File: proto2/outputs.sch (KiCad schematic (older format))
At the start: 36 parts, among them U1 AQY282SX, U10 AQY282SX, U11 AQY282SX, U12 AQY282SX, U2 AQY282SX, U3 AQY282SX, U4 AQY282SX, U5 AQY282SX, U6 AQY282SX, U7 AQY282SX, U8 AQY282SX, U9 AQY282SX

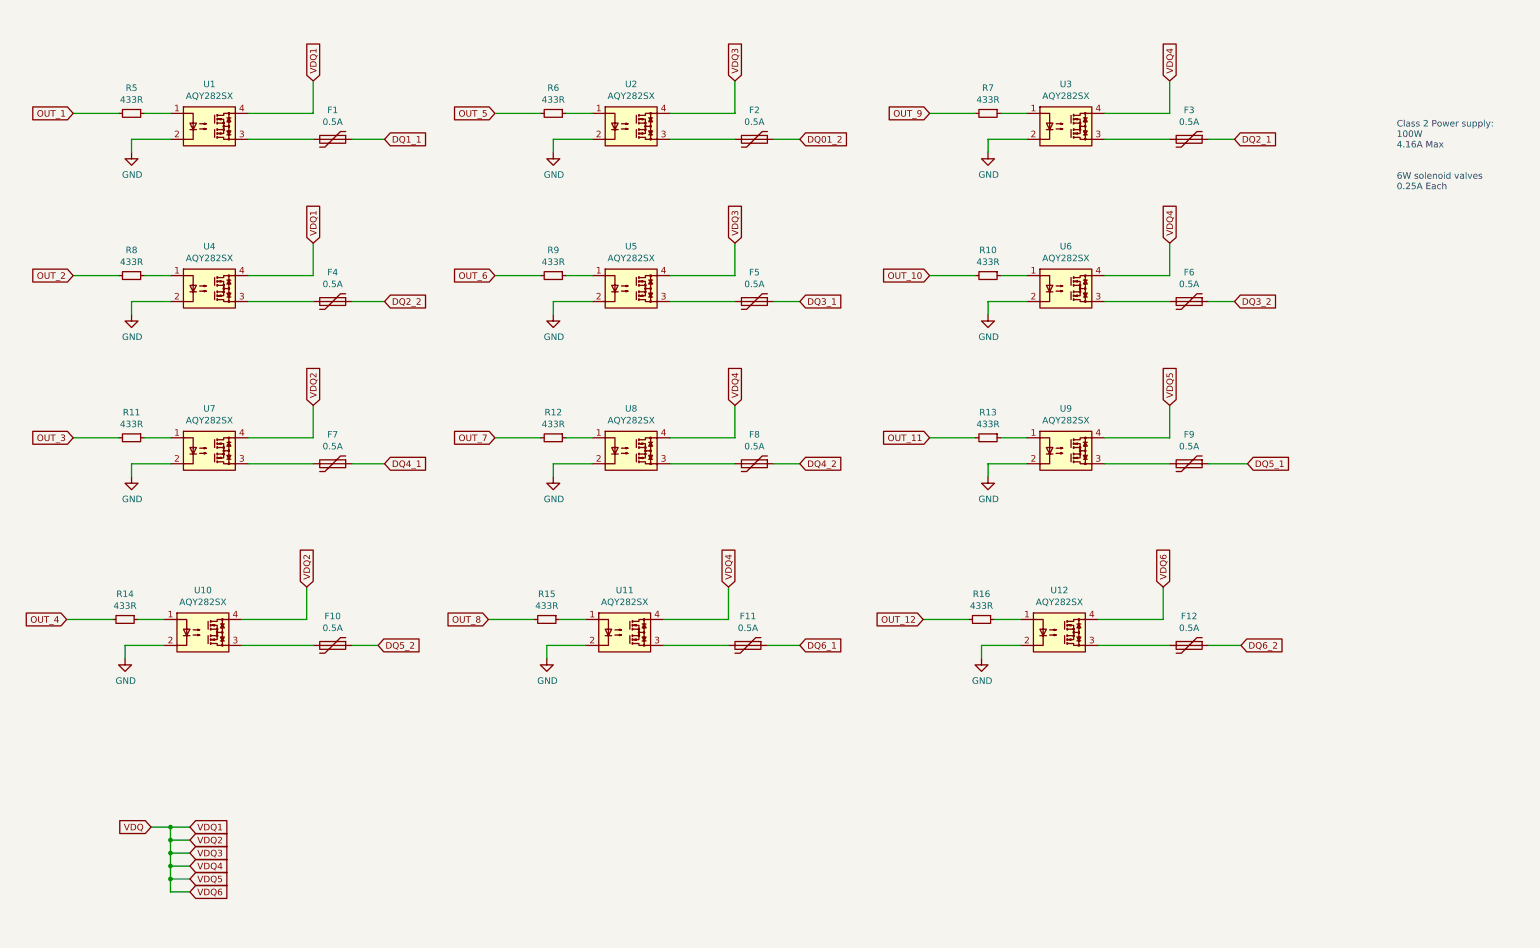
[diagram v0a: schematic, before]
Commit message: Routed Board.
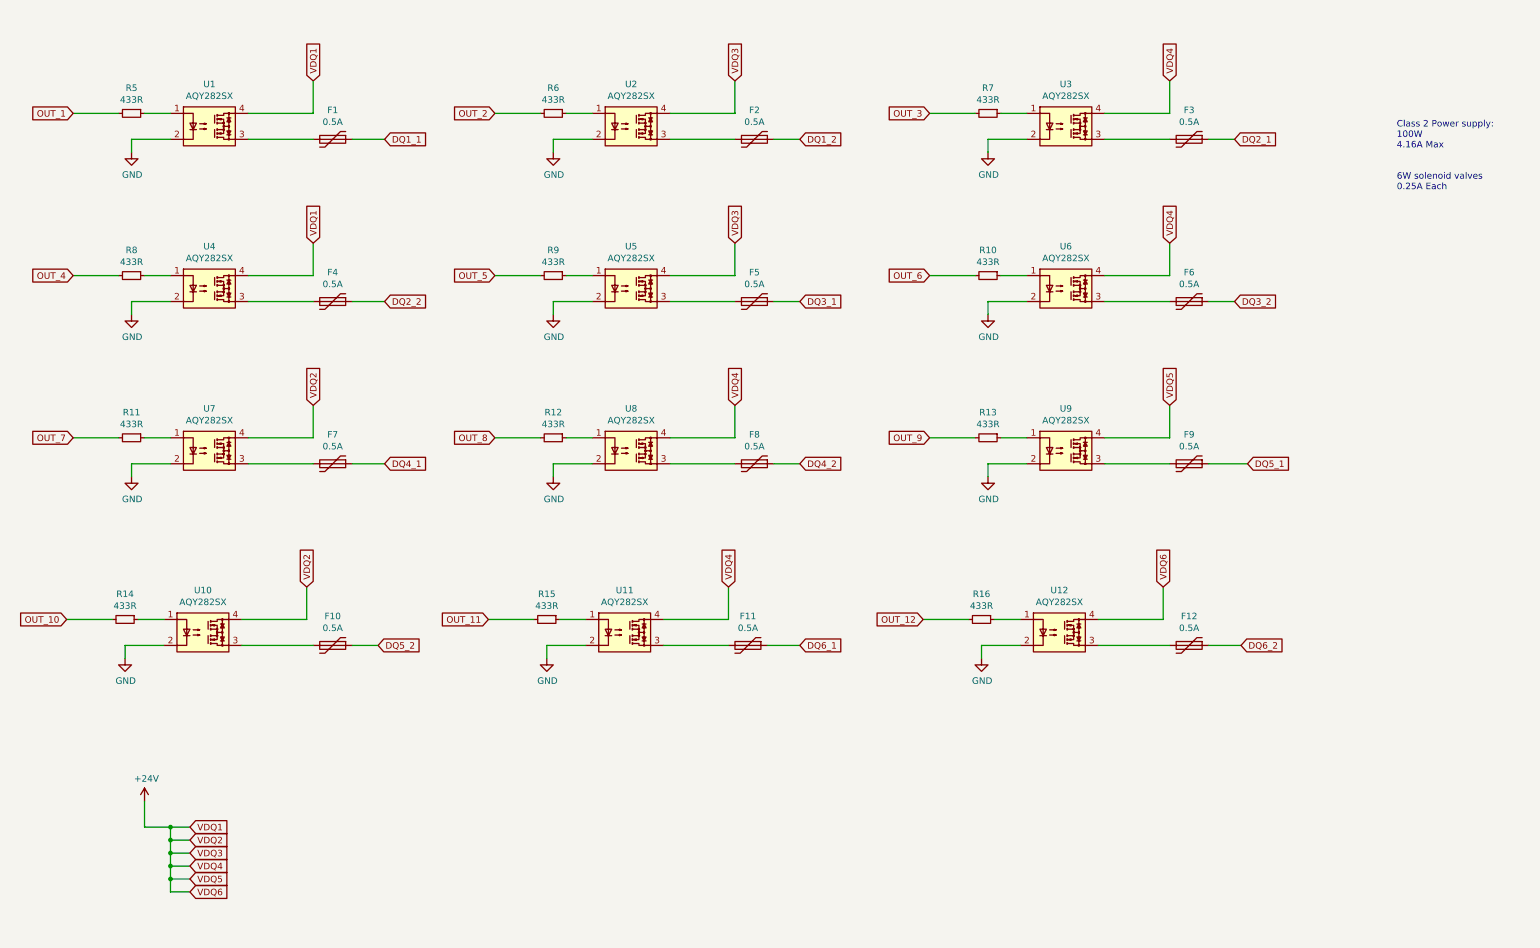
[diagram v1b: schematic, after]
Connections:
- net OUT_10: now also R14.2; no longer R10.2
- net OUT_11: now also R15.2; no longer R13.2
- net OUT_2: now also R6.2; no longer R8.2
- net OUT_3: now also R7.2; no longer R11.2
- net OUT_4: now also R8.2; no longer R14.2
- net OUT_5: now also R9.2; no longer R6.2
- net OUT_6: now also R10.2; no longer R9.2
- net OUT_7: now also R11.2; no longer R12.2
- net OUT_8: now also R12.2; no longer R15.2
- net OUT_9: now also R13.2; no longer R7.2
- net DQ01_2 renamed DQ1_2
- net VDQ renamed +24V
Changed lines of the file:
@@
 Sheet 2 4
 Title ""
-Date ""
+Date "2021-12-14"
 Rev ""
-Comp ""
+Comp "Langhe Greenhaus"
 Comment1 ""
 Comment2 ""
@@
 	2300 2850 2800 2850
 Text GLabel 6550 1600 2    50   Input ~ 0
-DQ01_2
-Text GLabel 950  2650 0    50   Input ~ 0
+DQ1_2
+Text GLabel 4200 1400 0    50   Input ~ 0
 OUT_2
 $Comp
@@
 Text GLabel 9900 1600 2    50   Input ~ 0
 DQ2_1
-Text GLabel 950  3900 0    50   Input ~ 0
+Text GLabel 7550 1400 0    50   Input ~ 0
 OUT_3
 $Comp
@@
 Text GLabel 3350 2850 2    50   Input ~ 0
 DQ2_2
-Text GLabel 900  5300 0    50   Input ~ 0
+Text GLabel 950  2650 0    50   Input ~ 0
 OUT_4
 $Comp
@@
 Wire Wire Line
 	4750 1400 4950 1400
-Text GLabel 4200 1400 0    50   Input ~ 0
+Text GLabel 4200 2650 0    50   Input ~ 0
 OUT_5
 $Comp
@@
 Wire Wire Line
 	4750 2650 4950 2650
-Text GLabel 4200 2650 0    50   Input ~ 0
+Text GLabel 7550 2650 0    50   Input ~ 0
 OUT_6
 $Comp
@@
 Wire Wire Line
 	4750 3900 4950 3900
-Text GLabel 4200 3900 0    50   Input ~ 0
+Text GLabel 950  3900 0    50   Input ~ 0
 OUT_7
 $Comp
@@
 	1    0    0    -1
 $EndComp
-Text GLabel 4150 5300 0    50   Input ~ 0
+Text GLabel 4200 3900 0    50   Input ~ 0
 OUT_8
 Text GLabel 2750 5050 1    50   Input ~ 0
@@
 	0    1    1    0
 $EndComp
-Text GLabel 1550 6900 0    50   Input ~ 0
-VDQ
 Text GLabel 1850 6900 2    50   Input ~ 0
 VDQ1
@@
 	1700 7200 1700 7100
 Wire Wire Line
-	1700 6900 1550 6900
-Wire Wire Line
 	1700 6900 1850 6900
 Connection ~ 1700 6900
@@
 Wire Wire Line
 	7900 1400 7550 1400
-Text GLabel 7550 1400 0    50   Input ~ 0
+Text GLabel 7550 3900 0    50   Input ~ 0
 OUT_9
 $Comp
@@
 Wire Wire Line
 	7900 2650 7550 2650
-Text GLabel 7550 2650 0    50   Input ~ 0
+Text GLabel 900  5300 0    50   Input ~ 0
 OUT_10
 $Comp
@@
 Wire Wire Line
 	7900 3900 7550 3900
-Text GLabel 7550 3900 0    50   Input ~ 0
+Text GLabel 4150 5300 0    50   Input ~ 0
 OUT_11
 $Comp
@@
 	1    0    0    -1
 $EndComp
+$Comp
+L power:+24V #PWR0124
+U 1 1 61C913D6
+P 1500 6700
+F 0 "#PWR0124" H 1500 6550 50  0001 C CNN
+F 1 "+24V" H 1515 6873 50  0000 C CNN
+F 2 "" H 1500 6700 50  0001 C CNN
+F 3 "" H 1500 6700 50  0001 C CNN
+	1    1500 6700
+	1    0    0    -1
+$EndComp
+Wire Wire Line
+	1500 6900 1500 6700
+Wire Wire Line
+	1500 6900 1700 6900
 $EndSCHEMATC

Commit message: Finished routing board and other changes, bad commit message, I know.
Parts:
- F1, F10, F11, F12, F2, F3, F4, F5, F6, F7, F8, F9: LCSC (none) -> C70070
- R10, R11, R12, R13, R14, R15, R16, R5, R6, R7, R8, R9: LCSC (none) -> C17694
- U1, U10, U11, U12, U2, U3, U4, U5, U6, U7, U8, U9: LCSC (none) -> C250827
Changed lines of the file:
@@
 F 2 "Package_SO:SO-4_4.4x4.3mm_P2.54mm" H 1800 1300 50  0001 L CIN
 F 3 "https://docs.broadcom.com/docs/AV02-0173EN" H 2000 1500 50  0001 L CNN
+F 4 "C250827" H 2000 1500 50  0001 C CNN "LCSC"
 	1    2000 1500
 	1    0    0    -1
@@
 F 2 "Package_SO:SO-4_4.4x4.3mm_P2.54mm" H 1800 2550 50  0001 L CIN
 F 3 "https://docs.broadcom.com/docs/AV02-0173EN" H 2000 2750 50  0001 L CNN
+F 4 "C250827" H 2000 2750 50  0001 C CNN "LCSC"
 	1    2000 2750
 	1    0    0    -1
@@
 F 2 "Package_SO:SO-4_4.4x4.3mm_P2.54mm" H 1800 3800 50  0001 L CIN
 F 3 "https://docs.broadcom.com/docs/AV02-0173EN" H 2000 4000 50  0001 L CNN
+F 4 "C250827" H 2000 4000 50  0001 C CNN "LCSC"
 	1    2000 4000
 	1    0    0    -1
@@
 F 2 "Package_SO:SO-4_4.4x4.3mm_P2.54mm" H 1750 5200 50  0001 L CIN
 F 3 "https://docs.broadcom.com/docs/AV02-0173EN" H 1950 5400 50  0001 L CNN
+F 4 "C250827" H 1950 5400 50  0001 C CNN "LCSC"
 	1    1950 5400
 	1    0    0    -1
@@
 F 2 "Package_SO:SO-4_4.4x4.3mm_P2.54mm" H 5050 1300 50  0001 L CIN
 F 3 "https://docs.broadcom.com/docs/AV02-0173EN" H 5250 1500 50  0001 L CNN
+F 4 "C250827" H 5250 1500 50  0001 C CNN "LCSC"
 	1    5250 1500
 	1    0    0    -1
@@
 F 2 "Package_SO:SO-4_4.4x4.3mm_P2.54mm" H 5050 2550 50  0001 L CIN
 F 3 "https://docs.broadcom.com/docs/AV02-0173EN" H 5250 2750 50  0001 L CNN
+F 4 "C250827" H 5250 2750 50  0001 C CNN "LCSC"
 	1    5250 2750
 	1    0    0    -1
@@
 F 2 "Package_SO:SO-4_4.4x4.3mm_P2.54mm" H 5050 3800 50  0001 L CIN
 F 3 "https://docs.broadcom.com/docs/AV02-0173EN" H 5250 4000 50  0001 L CNN
+F 4 "C250827" H 5250 4000 50  0001 C CNN "LCSC"
 	1    5250 4000
 	1    0    0    -1
@@
 F 2 "Package_SO:SO-4_4.4x4.3mm_P2.54mm" H 5000 5200 50  0001 L CIN
 F 3 "https://docs.broadcom.com/docs/AV02-0173EN" H 5200 5400 50  0001 L CNN
+F 4 "C250827" H 5200 5400 50  0001 C CNN "LCSC"
 	1    5200 5400
 	1    0    0    -1
@@
 F 2 "Resistor_SMD:R_1206_3216Metric" H 3000 1400 50  0001 L CNN
 F 3 "~" H 2950 1600 50  0001 C CNN
+F 4 "C70070" H 2950 1600 50  0001 C CNN "LCSC"
 	1    2950 1600
 	0    1    1    0
@@
 F 2 "Resistor_SMD:R_1206_3216Metric" H 3000 2650 50  0001 L CNN
 F 3 "~" H 2950 2850 50  0001 C CNN
+F 4 "C70070" H 2950 2850 50  0001 C CNN "LCSC"
 	1    2950 2850
 	0    1    1    0
@@
 F 2 "Resistor_SMD:R_1206_3216Metric" H 3000 3900 50  0001 L CNN
 F 3 "~" H 2950 4100 50  0001 C CNN
+F 4 "C70070" H 2950 4100 50  0001 C CNN "LCSC"
 	1    2950 4100
 	0    1    1    0
@@
 F 2 "Resistor_SMD:R_1206_3216Metric" H 3000 5300 50  0001 L CNN
 F 3 "~" H 2950 5500 50  0001 C CNN
+F 4 "C70070" H 2950 5500 50  0001 C CNN "LCSC"
 	1    2950 5500
 	0    1    1    0
@@
 F 2 "Resistor_SMD:R_1206_3216Metric" H 6250 1400 50  0001 L CNN
 F 3 "~" H 6200 1600 50  0001 C CNN
+F 4 "C70070" H 6200 1600 50  0001 C CNN "LCSC"
 	1    6200 1600
 	0    1    1    0
@@
 F 2 "Resistor_SMD:R_1206_3216Metric" H 6250 2650 50  0001 L CNN
 F 3 "~" H 6200 2850 50  0001 C CNN
+F 4 "C70070" H 6200 2850 50  0001 C CNN "LCSC"
 	1    6200 2850
 	0    1    1    0
@@
 F 2 "Resistor_SMD:R_1206_3216Metric" H 6250 3900 50  0001 L CNN
 F 3 "~" H 6200 4100 50  0001 C CNN
+F 4 "C70070" H 6200 4100 50  0001 C CNN "LCSC"
 	1    6200 4100
 	0    1    1    0
@@
 F 2 "Resistor_SMD:R_1206_3216Metric" H 6200 5300 50  0001 L CNN
 F 3 "~" H 6150 5500 50  0001 C CNN
+F 4 "C70070" H 6150 5500 50  0001 C CNN "LCSC"
 	1    6150 5500
 	0    1    1    0
@@
 F 2 "Package_SO:SO-4_4.4x4.3mm_P2.54mm" H 8400 1300 50  0001 L CIN
 F 3 "https://docs.broadcom.com/docs/AV02-0173EN" H 8600 1500 50  0001 L CNN
+F 4 "C250827" H 8600 1500 50  0001 C CNN "LCSC"
 	1    8600 1500
 	1    0    0    -1
@@
 F 2 "Package_SO:SO-4_4.4x4.3mm_P2.54mm" H 8400 2550 50  0001 L CIN
 F 3 "https://docs.broadcom.com/docs/AV02-0173EN" H 8600 2750 50  0001 L CNN
+F 4 "C250827" H 8600 2750 50  0001 C CNN "LCSC"
 	1    8600 2750
 	1    0    0    -1
@@
 F 2 "Package_SO:SO-4_4.4x4.3mm_P2.54mm" H 8400 3800 50  0001 L CIN
 F 3 "https://docs.broadcom.com/docs/AV02-0173EN" H 8600 4000 50  0001 L CNN
+F 4 "C250827" H 8600 4000 50  0001 C CNN "LCSC"
 	1    8600 4000
 	1    0    0    -1
@@
 F 2 "Resistor_SMD:R_0805_2012Metric" H 8000 3900 50  0001 C CNN
 F 3 "~" H 8000 3900 50  0001 C CNN
+F 4 "C17694" H 8000 3900 50  0001 C CNN "LCSC"
 	1    8000 3900
 	0    1    1    0
@@
 F 2 "Package_SO:SO-4_4.4x4.3mm_P2.54mm" H 8350 5200 50  0001 L CIN
 F 3 "https://docs.broadcom.com/docs/AV02-0173EN" H 8550 5400 50  0001 L CNN
+F 4 "C250827" H 8550 5400 50  0001 C CNN "LCSC"
 	1    8550 5400
 	1    0    0    -1
@@
 F 2 "Resistor_SMD:R_1206_3216Metric" H 9600 1400 50  0001 L CNN
 F 3 "~" H 9550 1600 50  0001 C CNN
+F 4 "C70070" H 9550 1600 50  0001 C CNN "LCSC"
 	1    9550 1600
 	0    1    1    0
@@
 F 2 "Resistor_SMD:R_1206_3216Metric" H 9600 2650 50  0001 L CNN
 F 3 "~" H 9550 2850 50  0001 C CNN
+F 4 "C70070" H 9550 2850 50  0001 C CNN "LCSC"
 	1    9550 2850
 	0    1    1    0
@@
 F 2 "Resistor_SMD:R_1206_3216Metric" H 9600 3900 50  0001 L CNN
 F 3 "~" H 9550 4100 50  0001 C CNN
+F 4 "C70070" H 9550 4100 50  0001 C CNN "LCSC"
 	1    9550 4100
 	0    1    1    0
@@
 F 2 "Resistor_SMD:R_1206_3216Metric" H 9600 5300 50  0001 L CNN
 F 3 "~" H 9550 5500 50  0001 C CNN
+F 4 "C70070" H 9550 5500 50  0001 C CNN "LCSC"
 	1    9550 5500
 	0    1    1    0
@@
 F 2 "Resistor_SMD:R_0805_2012Metric" H 7950 5300 50  0001 C CNN
 F 3 "~" H 7950 5300 50  0001 C CNN
+F 4 "C17694" H 7950 5300 50  0001 C CNN "LCSC"
 	1    7950 5300
 	0    1    1    0
@@
 F 2 "Resistor_SMD:R_0805_2012Metric" H 8000 2650 50  0001 C CNN
 F 3 "~" H 8000 2650 50  0001 C CNN
+F 4 "C17694" H 8000 2650 50  0001 C CNN "LCSC"
 	1    8000 2650
 	0    1    1    0
@@
 F 2 "Resistor_SMD:R_0805_2012Metric" H 8000 1400 50  0001 C CNN
 F 3 "~" H 8000 1400 50  0001 C CNN
+F 4 "C17694" H 8000 1400 50  0001 C CNN "LCSC"
 	1    8000 1400
 	0    1    1    0
@@
 F 2 "Resistor_SMD:R_0805_2012Metric" H 4650 3900 50  0001 C CNN
 F 3 "~" H 4650 3900 50  0001 C CNN
+F 4 "C17694" H 4650 3900 50  0001 C CNN "LCSC"
 	1    4650 3900
 	0    1    1    0
@@
 F 2 "Resistor_SMD:R_0805_2012Metric" H 4600 5300 50  0001 C CNN
 F 3 "~" H 4600 5300 50  0001 C CNN
+F 4 "C17694" H 4600 5300 50  0001 C CNN "LCSC"
 	1    4600 5300
 	0    1    1    0
@@
 F 2 "Resistor_SMD:R_0805_2012Metric" H 4650 2650 50  0001 C CNN
 F 3 "~" H 4650 2650 50  0001 C CNN
+F 4 "C17694" H 4650 2650 50  0001 C CNN "LCSC"
 	1    4650 2650
 	0    1    1    0
@@
 F 2 "Resistor_SMD:R_0805_2012Metric" H 4650 1400 50  0001 C CNN
 F 3 "~" H 4650 1400 50  0001 C CNN
+F 4 "C17694" H 4650 1400 50  0001 C CNN "LCSC"
 	1    4650 1400
 	0    1    1    0
@@
 F 2 "Resistor_SMD:R_0805_2012Metric" H 1400 3900 50  0001 C CNN
 F 3 "~" H 1400 3900 50  0001 C CNN
+F 4 "C17694" H 1400 3900 50  0001 C CNN "LCSC"
 	1    1400 3900
 	0    1    1    0
@@
 F 2 "Resistor_SMD:R_0805_2012Metric" H 1350 5300 50  0001 C CNN
 F 3 "~" H 1350 5300 50  0001 C CNN
+F 4 "C17694" H 1350 5300 50  0001 C CNN "LCSC"
 	1    1350 5300
 	0    1    1    0
@@
 F 2 "Resistor_SMD:R_0805_2012Metric" H 1400 2650 50  0001 C CNN
 F 3 "~" H 1400 2650 50  0001 C CNN
+F 4 "C17694" H 1400 2650 50  0001 C CNN "LCSC"
 	1    1400 2650
 	0    1    1    0
@@
 F 2 "Resistor_SMD:R_0805_2012Metric" H 1400 1400 50  0001 C CNN
 F 3 "~" H 1400 1400 50  0001 C CNN
+F 4 "C17694" H 1400 1400 50  0001 C CNN "LCSC"
 	1    1400 1400
 	0    1    1    0
